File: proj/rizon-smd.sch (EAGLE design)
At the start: 32 parts, among them J1 PWRJACK5521, P1 ADDR, P2 DATA, P3 CTL, P4 PWR, P6 10k, SW1 TACTSWTH6MM, U1 Z8400PLCC, U2 AS6C62256PDIP, U3 AS6C62256PDIP, U5 AT28C64BPLCC, U7 7805TO220, U9 7400PDIP, X1 4.0Mhz

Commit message: Started SMD version of Rizon Computer Cleaned up library
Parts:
- removed P2: DATA, dooba:PIN_8
- removed P3: CTL, dooba:PIN_16
- removed P4: PWR, dooba:PIN_4
- removed SW1: TACTSWTH6MM, dooba:TACTSWTH6MM
- added B1: TACTSW_2MICRO3X6, dooba:TACTSW_2MICRO3X6
- added C19, C21, C22, C23, C24, C25, C26: 1uF, dooba:CAP0805
- added C20, C27: 100nF, dooba:CAP0805
- added J2: DB9A-DS09AKG, dooba:DB9A-DS09AKG
- added U10: 7432SOIC, dooba:7432SOIC
- added U11: 74138SOIC, dooba:74138SOIC
- added U12: 7400SOIC, dooba:7400SOIC
- added U13, U14: 74590SOIC, dooba:74590SOIC
- added U15: 74273DW, dooba:74273DW
- added U16, U4: PC16550DPLCC-SMD, dooba:PC16550DPLCC-SMD
- added U8: MAX232NNS, dooba:MAX232NNS
- added X2: 18.432Mhz, dooba:OSC4_OESMD-7X5
- C1, C3: device dooba:CAP_POLARIZEDRAD_5MM -> dooba:CAP1210
- C10, C14, C4, C5, C6, C8: device dooba:CAP508 -> dooba:CAP0805
- C11, C15, C7, C9: device dooba:CAPDISC -> dooba:CAP0805
- C2: device dooba:CAP_POLARIZEDRAD_5MM -> dooba:CAP0805
- D1, D2: device dooba:LED5MM -> dooba:LED0805
- P1: value ADDR -> UART1(GND-TX-RX); device dooba:PIN_16 -> dooba:PIN_3
- R1, R2: device dooba:RES8MM -> dooba:RES0805
- S1: value SWITCH_SPDT2EG1271 -> SWITCH_SPDT; device dooba:SWITCH_SPDT2EG1271 -> dooba:SWITCH_SPDT
- U1: value Z8400PLCC -> Z8400LQFP; device dooba:Z8400PLCC -> dooba:Z8400LQFP
- U2, U3: value AS6C62256PDIP -> AS6C62256SOP28; device dooba:AS6C62256PDIP -> dooba:AS6C62256SOP28
- U7: value 7805TO220 -> NCP1117SOT223; device dooba:7805TO220 -> dooba:NCP1117SOT223
- U9: value 7400PDIP -> 7400SOIC; device dooba:7400PDIP -> dooba:7400SOIC
- X1: device dooba:OSC412.7 -> dooba:OSC4_OESMD-7X5
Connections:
- new net !IODEV0: U10.3A, U11.Y0
- new net !IODEV1: U11.Y1, U4.!CS2
- new net !IODEV2: U11.Y2, U16.!CS2
- new net !IODEV3: U11.Y3
- new net !IODEV4: U11.Y4
- new net !IODEV5: U11.Y5
- new net !IODEV6: U11.Y6
- new net !IODEV7: U11.Y7
- new net !SCR0_CP: U10.3Y, U12.3A, U12.3B
- new net !TIMER_CLR: U13.!CCLR, U14.!CCLR, U15.Q2
- new net CLK_UART: U16.XIN, U4.XIN, X2.OUT
- new net CLK_UART0_RX: U4.!BAUDOUT, U4.RCLK
- new net CLK_UART1_RX: U16.!BAUDOUT, U16.RCLK
- new net INT_DEV: U10.2Y, U12.2A
- new net INT_EN: U12.2B, U15.Q1
- new net INT_TIMER: U10.2B
- new net INT_UART: U10.1Y, U10.2A
- new net INT_UART0: U10.1A, U4.INTR
- new net INT_UART1: U10.1B, U16.INTR
- new net N$10: C25.2, U8.VS-
- new net N$11: J2.TXD, U8.T1OUT
- new net N$12: J2.RXD, U8.R1IN
- new net N$3: U13.!RCO, U14.!CCKEN
- new net N$5: C24.2, U8.C2+
- new net N$6: C24.1, U8.C2-
- new net N$7: C22.1, U8.C1-
- new net N$8: C22.2, U8.C1+
- new net N$9: C23.1, U8.VS+
- new net RESET: U12.1Y, U16.MR, U4.MR
- new net SCR0_CP: U12.3Y, U15.CP
- new net TIMER_OUT: U14.Q7
- new net UART0_RX: U4.SIN, U8.R1OUT
- new net UART0_TX: U4.SOUT, U8.T1IN
- new net UART1_RX: P1.3, U16.SIN
- new net UART1_TX: P1.2, U16.SOUT
- net !BUSACK: no longer P3.7
- net !BUSREQ: no longer P3.3
- net !HALT: no longer P3.10
- net !INT: now also U12.2Y; no longer P3.12
- net !IORQ: now also U11.!G2A, U11.!G2B; no longer P3.8
- net !M1: now also U11.G1; no longer P3.1
- net !MREQ: no longer P3.11
- net !NMI: no longer P3.13
- net !RD: now also U16.!RD, U4.!RD; no longer P3.9
- net !RESET: now also B1.1, U12.1A, U12.1B, U15.!MR; no longer P3.4, SW1.3
- net !RFSH: no longer P3.2
- net !ROM_EN: now also U15.Q0; no longer P3.14
- net !WAIT: no longer P3.5
- net !WR: now also U10.3B, U16.!WR, U4.!WR; no longer P3.6
- net ADDR0: now also U16.A0, U4.A0; no longer P1.1
- net ADDR1: now also U16.A1, U4.A1; no longer P1.2
- net ADDR10: no longer P1.11
- net ADDR11: no longer P1.12
- net ADDR12: no longer P1.13
- net ADDR13: now also U11.A; no longer P1.14
- net ADDR14: now also U11.B; no longer P1.15
- net ADDR15: now also U11.C; no longer P1.16
- net ADDR2: now also U16.A2, U4.A2; no longer P1.3
- net ADDR3: no longer P1.4
- net ADDR4: no longer P1.5
- net ADDR5: no longer P1.6
- net ADDR6: no longer P1.7
- net ADDR7: no longer P1.8
- net ADDR8: no longer P1.9
- net ADDR9: no longer P1.10
- net CLK: now also U13.CCLK, U13.RCLK, U14.CCLK, U14.RCLK; no longer P3.15
- net DATA0: now also U15.D0, U16.D0, U4.D0; no longer P2.1
- net DATA1: now also U15.D1, U16.D1, U4.D1; no longer P2.2
- net DATA2: now also U15.D2, U16.D2, U4.D2; no longer P2.3
- net DATA3: now also U15.D3, U16.D3, U4.D3; no longer P2.4
- net DATA4: now also U15.D4, U16.D4, U4.D4; no longer P2.5
- net DATA5: now also U15.D5, U16.D5, U4.D5; no longer P2.6
- net DATA6: now also U15.D6, U16.D6, U4.D6; no longer P2.7
- net DATA7: now also U15.D7, U16.D7, U4.D7; no longer P2.8
- net GND: now also B1.2, C19.1, C20.1, C21.1, C25.1, C26.1, C27.1, J2.GND, P1.1, U10.GND, U11.GND, U12.GND, U13.!CCKEN, U13.!OE, U13.GND, U14.!OE, U14.GND, U15.GND, U16.!ADS, U16.GND, U16.RD, U16.WR, U4.!ADS, U4.GND, U4.RD, U4.WR, U8.GND, X2.GND; no longer P3.16, P4.1, P4.3, SW1.1
- net N$4: no longer S1.4
- net VCC: now also C19.2, C20.2, C21.2, C23.2, C26.2, C27.2, U10.VCC, U11.VCC, U12.VCC, U13.VCC, U14.VCC, U15.VCC, U16.CS0, U16.CS1, U16.VCC, U4.CS0, U4.CS1, U4.VCC, U7.VOUT@PAD, U8.VCC, X1.OE, X2.OE, X2.VCC; no longer P4.4
- net VIN: no longer P4.2, S1.5
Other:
- note added: "Glue Logic"
- note added: "IO Device Selector"
- note added: "Interrupt Logic"
- note added: "SCR0 - System Control Register 0"
- note added: "Serial Port 0"
- note added: "Serial Port 1"
- note added: "System Timer"
- note added: "UART Clock Source"
- note removed: "Connectors"
- moved on the sheet: C4, C5, D1, D2, J1, R1, R2

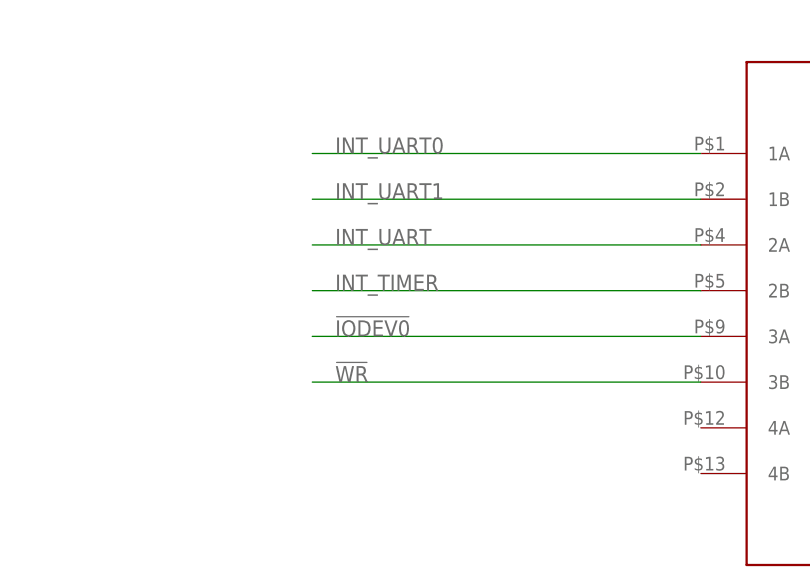
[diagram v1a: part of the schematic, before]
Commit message: Added missing signal net (TIMER_OUT -> INT_TIMER) in Rizon I/O board Further routed SMD version of Rizon computer
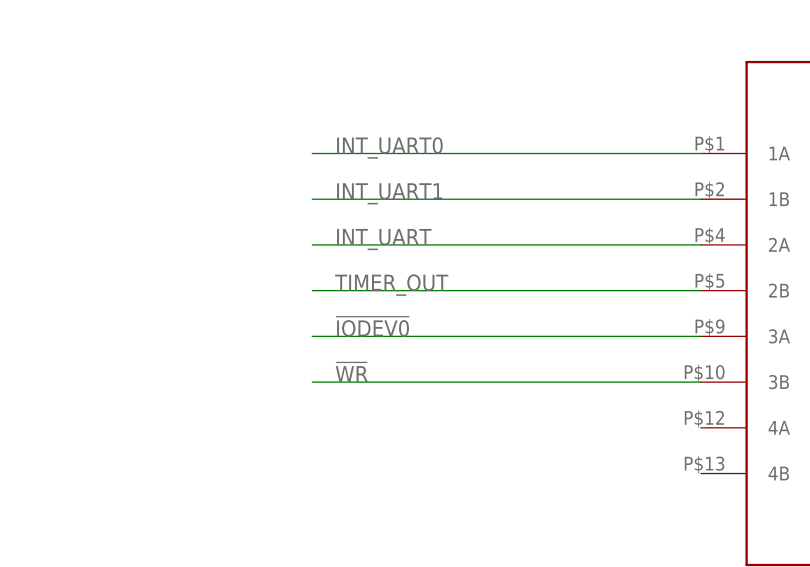
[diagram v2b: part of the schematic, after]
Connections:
- removed net INT_TIMER: U10.2B
- net TIMER_OUT: now also U10.2B
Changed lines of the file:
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@@
 <label x="1145.54" y="78.74" size="1.778" layer="95"/>
 </segment>
-</net>
-<net name="INT_TIMER" class="0">
 <segment>
 <pinref part="U10" gate="U1" pin="2B"/>

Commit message: Added breakouts to Rizon SMD
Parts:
- added P2: ADDR, dooba:PIN_16
- added P3: DATA, dooba:PIN_8
- added P4: CTL, dooba:PIN_16
- added P5: PWR, dooba:PIN_4
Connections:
- net !BUSACK: now also P4.7
- net !BUSREQ: now also P4.3, P6.4; no longer P6.3
- net !HALT: now also P4.10
- net !INT: now also P4.12, P6.1; no longer P6.2
- net !IORQ: now also P4.8
- net !M1: now also P4.1
- net !MREQ: now also P4.11
- net !NMI: now also P4.13, P6.2; no longer P6.1
- net !RD: now also P4.9
- net !RESET: now also P4.4, P6.5; no longer P6.4
- net !RFSH: now also P4.2
- net !ROM_EN: now also P4.14
- net !WAIT: now also P4.5, P6.3; no longer P6.5
- net !WR: now also P4.6
- net ADDR0: now also P2.1
- net ADDR1: now also P2.2
- net ADDR10: now also P2.11
- net ADDR11: now also P2.12
- net ADDR12: now also P2.13
- net ADDR13: now also P2.14
- net ADDR14: now also P2.15
- net ADDR15: now also P2.16
- net ADDR2: now also P2.3
- net ADDR3: now also P2.4
- net ADDR4: now also P2.5
- net ADDR5: now also P2.6
- net ADDR6: now also P2.7
- net ADDR7: now also P2.8
- net ADDR8: now also P2.9
- net ADDR9: now also P2.10
- net CLK: now also P4.15
- net DATA0: now also P3.1
- net DATA1: now also P3.2
- net DATA2: now also P3.3
- net DATA3: now also P3.4
- net DATA4: now also P3.5
- net DATA5: now also P3.6
- net DATA6: now also P3.7
- net DATA7: now also P3.8
- net GND: now also P4.16, P5.1, P5.3
- net VCC: now also P5.4
- net VIN: now also P5.2

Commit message: Rizon SMD routing
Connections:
- net !BUSACK: now also P4.9; no longer P4.7
- net !BUSREQ: now also P4.10; no longer P4.3
- net !HALT: now also P4.5; no longer P4.10
- net !INT: now also P4.3; no longer P4.12
- net !IORQ: now also P4.7; no longer P4.8
- net !M1: now also P4.12; no longer P4.1
- net !MREQ: now also P4.6; no longer P4.11
- net !NMI: now also P4.4; no longer P4.13
- net !RD: now also P4.2; no longer P4.9
- net !RESET: now also P4.11; no longer P4.4
- net !RFSH: now also P4.13; no longer P4.2
- net !ROM_EN: now also P4.15; no longer P4.14
- net !WAIT: now also P4.8; no longer P4.5
- net !WR: now also P4.1; no longer P4.6
- net CLK: now also P4.14; no longer P4.15
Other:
- moved on the sheet: C19, C20, C21, C22, C23, C24, C25, C26, C27, J2, P1, P2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

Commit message: Completed Rizon SMD board
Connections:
- net !BUSREQ: now also P4.8; no longer P4.10
- net !HALT: now also P4.4; no longer P4.5
- net !INT: now also P4.1; no longer P4.3
- net !IORQ: now also P4.6; no longer P4.7
- net !MREQ: now also P4.5; no longer P4.6
- net !NMI: now also P4.2; no longer P4.4
- net !RD: now also P4.11; no longer P4.2
- net !RESET: now also P4.7; no longer P4.11
- net !WAIT: now also P4.3; no longer P4.8
- net !WR: now also P4.10; no longer P4.1
- net VIN: now also S1.3; no longer S1.2
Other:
- moved on the sheet: J1, S1
